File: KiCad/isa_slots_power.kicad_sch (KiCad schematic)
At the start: 68 parts, among them J2 BUSAT_HOST, J3 BUSAT_HOST, J4 BUSAT_HOST, J5 BUSAT_HOST, J6 BUSAT_HOST, J7 BUSAT_HOST, J8 AT_POWER1, J9 AT_POWER2

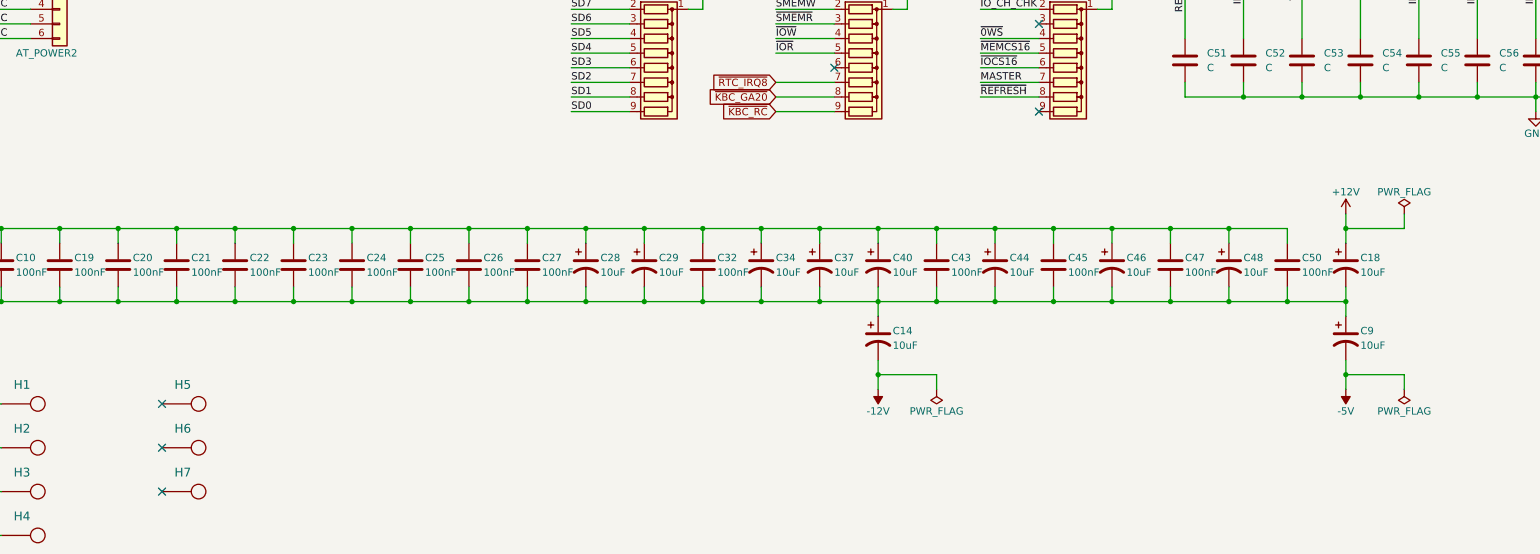
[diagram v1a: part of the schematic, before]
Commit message: Version 1.4: Move mounting holes to ATX compatible locations
Signed-off-by: Sergey Kiselev <skiselev@gmail.com>
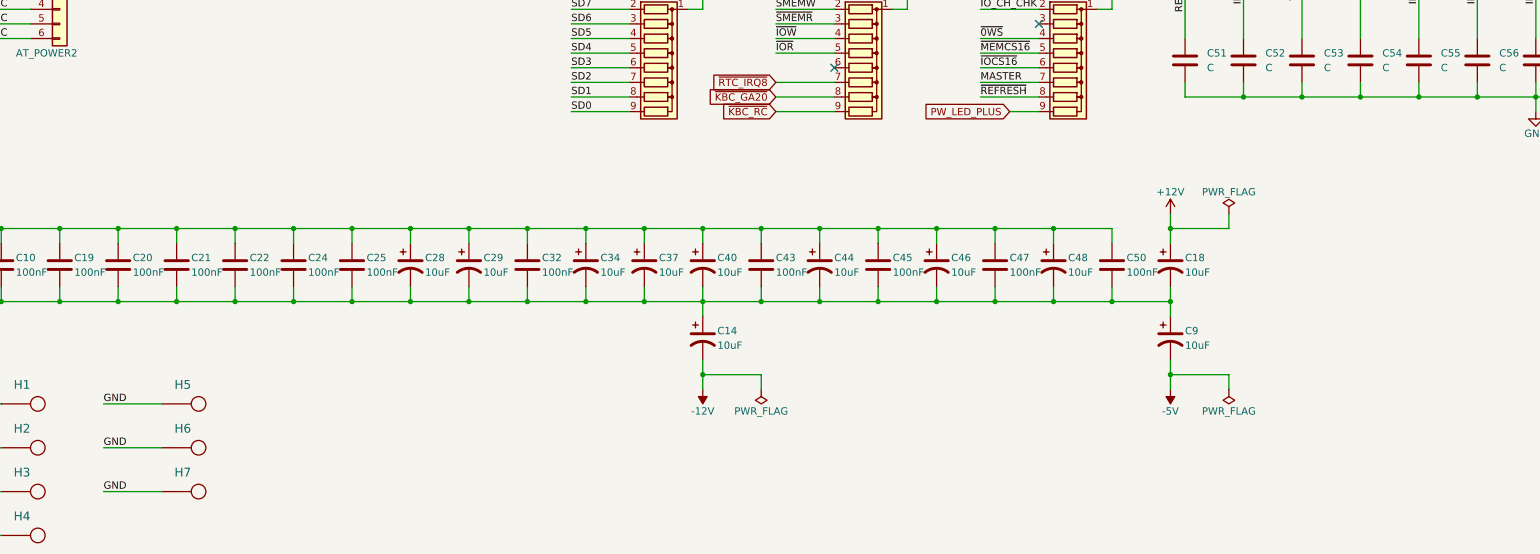
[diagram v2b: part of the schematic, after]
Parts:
- removed C23, C26, C27: 100nF, My_Components:Cap_Cer_508, symbol Device:C
- H5, H6, H7: footprint MountingHole:MountingHole_4mm -> MountingHole:MountingHole_4mm_Pad_Via
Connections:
- net GND: now also H5.1, H6.1, H7.1
- net PW_LED_PLUS: now reaches RP3.9 (R8)
- no-connect marks 6 -> 2
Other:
- moved on the sheet: C14, C18, C24, C25, C28, C29, C32, C34, C37, C40, C43, C44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

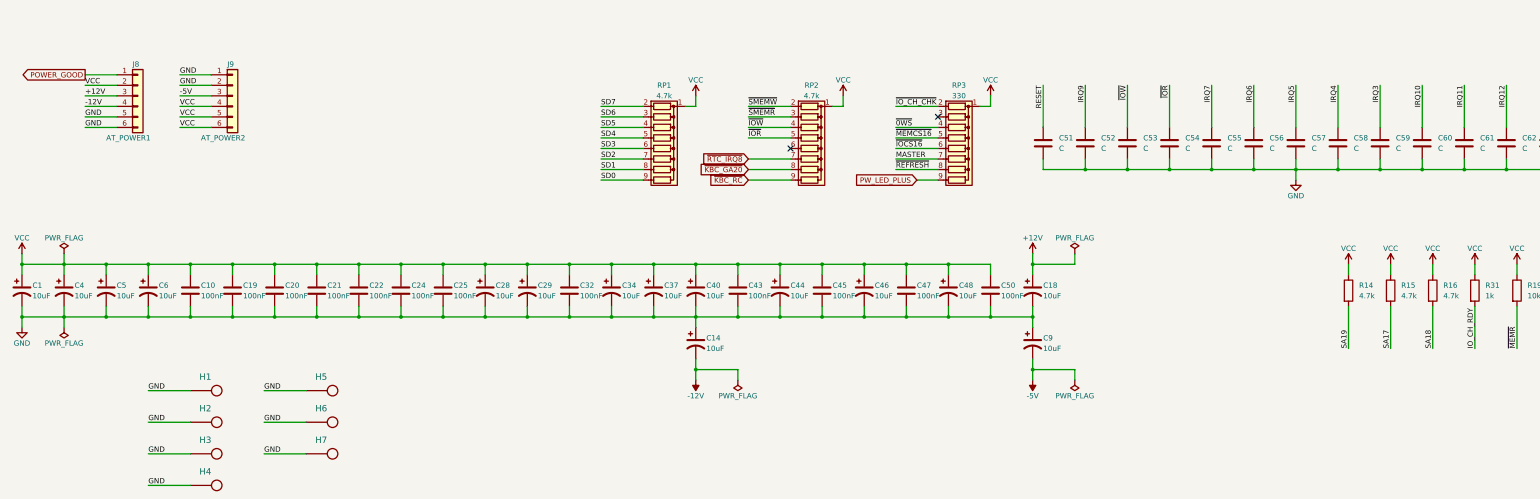
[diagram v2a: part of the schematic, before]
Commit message: Version 1.5: Add filtering capacitors
Signed-off-by: Sergey Kiselev <skiselev@gmail.com>
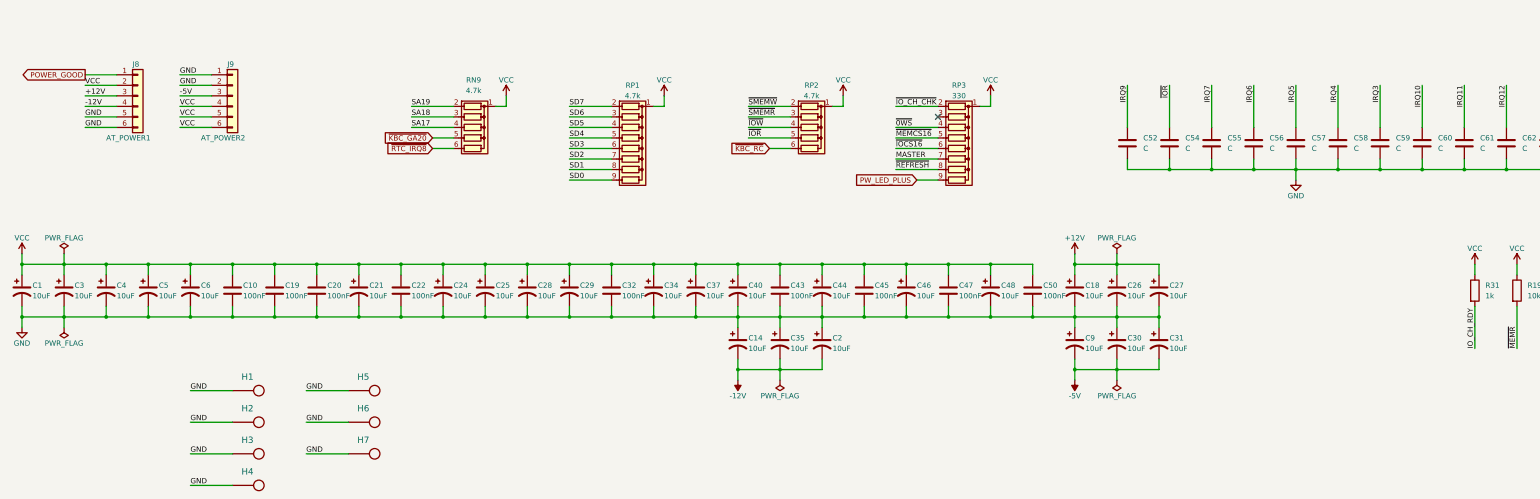
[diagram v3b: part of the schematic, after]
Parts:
- removed C21, C24, C25: 100nF, My_Components:Cap_Cer_508, symbol Device:C
- removed C51, C53: C, My_Components:Cap_Cer_508, symbol Device:C
- removed R14, R15, R16: 4.7k, My_Components:Res_Axial_L6.3mm_D2.5mm_P10.16mm_Horizontal, symbol Device:R
- removed RP2: 4.7k, My_Components:Conn_SIL9, symbol Device:R_Network08
- added C2, C21, C24, C25, C26, C27, C3, C30, C31, C35: 10uF, My_Components:Cap_Elec_Radial_5mm_2.5mm, symbol Device:C_Polarized_US
- added RN9, RP2: 4.7k, My_Components:Conn_SIL6, symbol Device:R_Network05
- R31: footprint My_Components:Res_Axial_L6.3mm_D2.5mm_P10.16mm_Horizontal -> My_Components:Res_762
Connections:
- net +12V: now also C26.1, C27.1
- net -12V: now also C2.2, C35.2
- net -5V: now also C30.2, C31.2
- net GND: now also C2.1, C21.2, C24.2, C25.2, C26.2, C27.2, C3.2, C30.1, C31.1, C35.1
- net SA17: now also RN9.4 (R3)
- net SA18: now also RN9.3 (R2)
- net SA19: now also RN9.2 (R1)
- net VCC: now also C21.1, C24.1, C25.1, C3.1, RN9.1 (common), RP2.1 (common)
- net ~{IOR}: now also RP2.5 (R4)
- net ~{IOW}: now also RP2.4 (R3)
- net ~{KBC_GA20}: now also RN9.5 (R4)
- net ~{KBC_RC}: now also RP2.6 (R5)
- net ~{RTC_IRQ8}: now also RN9.6 (R5)
- net ~{SMEMR}: now also RP2.3 (R2)
- net ~{SMEMW}: now also RP2.2 (R1)
- no-connect marks 2 -> 1
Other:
- moved on the sheet: C10, C14, C18, C19, C20, C22, C28, C29, C32, C34, C37, C4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

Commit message: Version 1.6: Use half-can oscillators and low-profile crystal
Signed-off-by: Sergey Kiselev <skiselev@gmail.com>
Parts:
- R19, R21: footprint My_Components:Res_Axial_L6.3mm_D2.5mm_P10.16mm_Horizontal -> My_Components:Res_762
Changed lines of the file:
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@@
       (effects (font (size 1.27 1.27)) (justify left))
     )
-    (property "Footprint" "My_Components:Res_Axial_L6.3mm_D2.5mm_P10.16mm_Horizontal" (id 2) (at 379.222 222.25 90)
+    (property "Footprint" "My_Components:Res_762" (id 2) (at 379.222 222.25 90)
       (effects (font (size 1.27 1.27)) hide)
     )
@@
       (effects (font (size 1.27 1.27)) (justify left))
     )
-    (property "Footprint" "My_Components:Res_Axial_L6.3mm_D2.5mm_P10.16mm_Horizontal" (id 2) (at 389.382 222.25 90)
-      (effects (font (size 1.27 1.27)) hide)
-    )
+    (property "Footprint" "My_Components:Res_762" (id 2) (at 389.382 222.25 90)
+      (effects (font (size 1.27 1.27)) hide)
+    )

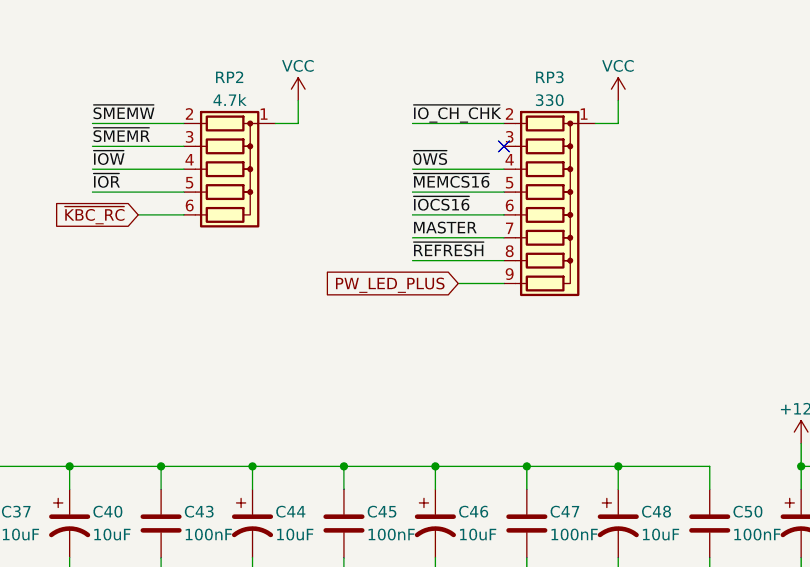
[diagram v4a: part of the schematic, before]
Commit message: Version 1.7: Use single front panel connector
Signed-off-by: Sergey Kiselev <skiselev@gmail.com>
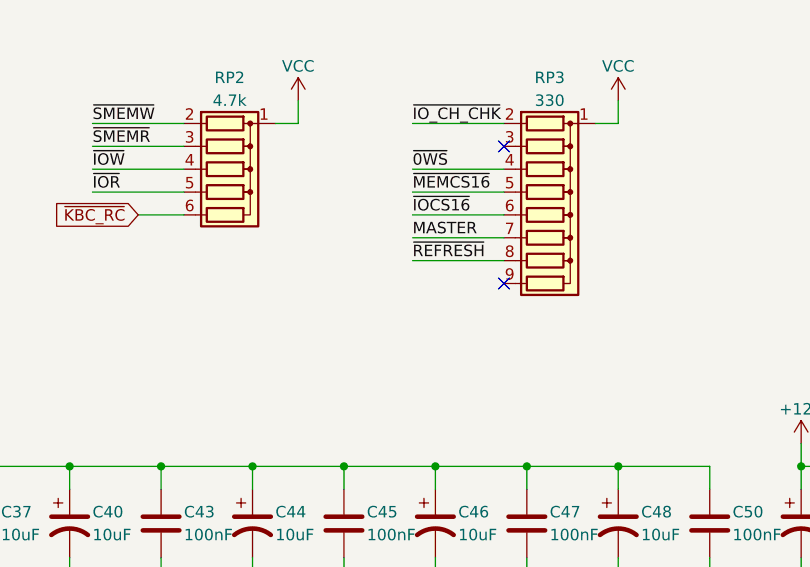
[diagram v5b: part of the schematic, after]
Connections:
- net PW_LED_PLUS: no longer names the net of RP3.9 (R8)
- no-connect marks 1 -> 2
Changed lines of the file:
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@@
   (junction (at 111.76 228.6) (diameter 0) (color 0 0 0 0)
   )
+  (no_connect (at 241.3 195.58))
   (no_connect (at 241.3 180.34))
   (wire (pts (xy 114.3 124.46) (xy 104.14 124.46))
@@
     (stroke (width 0) (type default) (color 0 0 0 0))
   )
-  (wire (pts (xy 236.22 195.58) (xy 241.3 195.58))
-    (stroke (width 0) (type default) (color 0 0 0 0))
-  )
   (wire (pts (xy 297.18 60.96) (xy 287.02 60.96))
     (stroke (width 0) (type default) (color 0 0 0 0))
@@
     )
   )
-  (global_label "PW_LED_PLUS" (shape input) (at 236.22 195.58 180) (fields_autoplaced)
-    (effects (font (size 1.27 1.27)) (justify right))
-    (property "Intersheet References" "${INTERSHEET_REFS}" (id 0) (at 220.865 195.5006 0)
-      (effects (font (size 1.27 1.27)) (justify right) hide)
-    )
-  )

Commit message: Version 1.9: Add pin headers for the CPU
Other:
- company: Sergey Kiselev -> Copyright (C) 2024-2026 Sergey Kiselev
- title: ISA Bus -> 386SX Motherboard Based on SARC RC2016 Chipset
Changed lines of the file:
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@@
   (paper "A3")
   (title_block
-    (title "ISA Bus")
-    (date "2024-02-14")
-    (company "Sergey Kiselev")
+    (title "386SX Motherboard Based on SARC RC2016 Chipset")
+    (date "2026-01-09")
+    (rev "1.9")
+    (company "Copyright (C) 2024-2026 Sergey Kiselev")
+    (comment 1 "https://github.com/Marco-Both/M396F-Replika")
+    (comment 2 "Based on the M396F motherboard replica by Marco Both:")
+    (comment 3 "https://github.com/skiselev/mb386sx-rc2016")
   )
   (junction (at 121.92 215.9) (diameter 0) (color 0 0 0 0)

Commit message: Use ATX power supply, add ATX power-on circuit
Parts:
- removed J8: AT_POWER1, My_Components:Conn_Power_AT_6pin, symbol Connector_Generic:Conn_01x06
- removed J9: AT_POWER2, My_Components:Conn_Power_AT_6pin, symbol Connector_Generic:Conn_01x06
- added C68, C69: 1uF, My_Components:Cap_Cer_508, symbol Device:C
- added C70, C71: 0.1uF, My_Components:Cap_Cer_508, symbol Device:C
- added D1: Power, My_Components:LED_3mm, symbol Device:LED
- added D2: Activity, My_Components:LED_3mm, symbol Device:LED_Dual_Bidirectional
- added J8: ATX_POWER_20, My_Components:Conn_Power_ATX_20pin, symbol my_components:ATX_POWER_20
- added R60, R62, R65: 470, My_Components:Res_762, symbol Device:R
- added R61: 1k, My_Components:Res_762, symbol Device:R
- added R63: 10k, My_Components:Res_762, symbol Device:R
- added R64: 20k, My_Components:Res_762, symbol Device:R
- added U14: LM7905, My_Components:IC_TO220-3_Vert, symbol Regulator_Linear:LM7905_TO220
- added U15: 74HCT14, My_Components:IC_DIP14_300, symbol 74xx:74LS14
- added U16: 74HCT74, My_Components:IC_DIP14_300, symbol 74xx:74LS74
- C52, C54, C55, C56, C57, C58, C59, C60, C61, C62, C63, C64: value C -> DNP
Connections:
- net +12V: now also J8.10 (12V)
- net -12V: now also J8.12 (-12V), U14.2 (VI)
- net -5V: now also U14.3 (VO)
- net GND: now also C68.2, C69.2, C70.2, C71.2, D1.1 (K), J8.13 (GND), J8.15 (GND), J8.16 (GND), J8.17 (GND), J8.3 (GND), J8.5 (GND), J8.7 (GND), U14.1 (GND), U15.7 (GND), U16.7 (GND)
- net POWER_GOOD: now also J8.8 (PWR_OK)
- net SA7: now also R61.1
- net VCC: now also J8.19 (5V), J8.20 (5V), J8.4 (5V), J8.6 (5V), R65.1
- new net: D2.1 (KA), U16.9 (Q)
- new net: D2.2 (AK), R60.2
- new net: C68.1, R62.2, U15.1
- new net: D1.2 (A), R65.2
- new net: C69.1, R64.1, U15.3
- new net: R61.2, U16.11 (C)
- new net: U15.4, U15.5
- new net: U15.6, U16.4 (~{S})
- new net: R60.1, U16.12 (D), U16.8 (~{Q})
- new net: U15.2, U16.3 (C)
- new net POWER_SW: R62.1, R63.1
- new net VSTB: C70.1, C71.1, J8.9 (5VSB), R63.2, R64.2, U15.11, U15.13, U15.14 (VCC), U15.9, U16.1 (~{R}), U16.10 (~{S}), U16.14 (VCC)
- new net ~{PS_OFF}: U16.13 (~{R}), U16.2 (D), U16.6 (~{Q})
- new net ~{PS_ON}: J8.14 (~{PS_ON}), U16.5 (Q)
- no-connect marks 2 -> 9
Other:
- moved on the sheet: C1, C10, C14, C18, C19, C2, C20, C21, C22, C24, C25, C26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

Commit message: Version 2.1: Reorder component references; Update silkscreen; Add signal names on the back silkscreen
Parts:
- C20: renamed from C70; value 0.1uF -> 100nF
- C21: renamed from C71; value 0.1uF -> 100uF
- J12: renamed from J8; value ATX_POWER_20 -> Power
- renumbered C45 to C11, C43 to C12, C32 to C13, C20 to C14, C47 to C15, C10 to C16, C19 to C17, C22 to C18, C50 to C19, C68 to C23, C69 to C24, C1 to C25, C48 to C26, C4 to C27, C25 to C28, C40 to C29, C24 to C30, C21 to C31, C5 to C32, C46 to C33, C6 to C34, C3 to C35, C29 to C36, C28 to C38, C44 to C39, C34 to C40, C26 to C41, C18 to C42, C27 to C43, C2 to C44, C14 to C45, C35 to C46, C30 to C47, C9 to C48, C31 to C49, C52 to C50, C54 to C51, C55 to C52, C56 to C53, C57 to C54, C58 to C55, C59 to C56, C60 to C57, C61 to C58, C62 to C59, C63 to C60, C64 to C61, J2 to J1, J3 to J2, J4 to J3, J5 to J4, J7 to J5, R65 to R27, R60 to R28, R62 to R29, R31 to R30, R61 to R31, R19 to R35, R21 to R36, R63 to R38, R64 to R39, RP3 to RN1, RP2 to RN2, RN9 to RN3, RP1 to RN4, U14 to U10, U15 to U8, U16 to U9
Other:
- moved on the sheet: C11, C12, C13, C14, C15, C18, C19, C25, C26, C27, C28, C29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
